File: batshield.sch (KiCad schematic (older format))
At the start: 79 parts, among them J1 mic in, J10 rigth donw pins, J11 service power, J2 Audio-Jack-2, J3 Audio-Jack-2, J4 left uppins, J5 left down pins, J6 Audio-Jack-2, J7 DIN-5_180degree, J8 DIN-5_180degree, J9 rigth up pins, SW1 SW_SPDT, SW10 SW_SPST, SW11 SW_SPST, SW12 SW_Push, SW2 SW_SPDT, SW3 SW_SPDT, SW4 SW_SPST, SW5 SW_Push, SW6 SW_SPST, SW7 SW_Push, SW8 SW_SPST, SW9 SW_Push, U1 LM741, U2 4N35

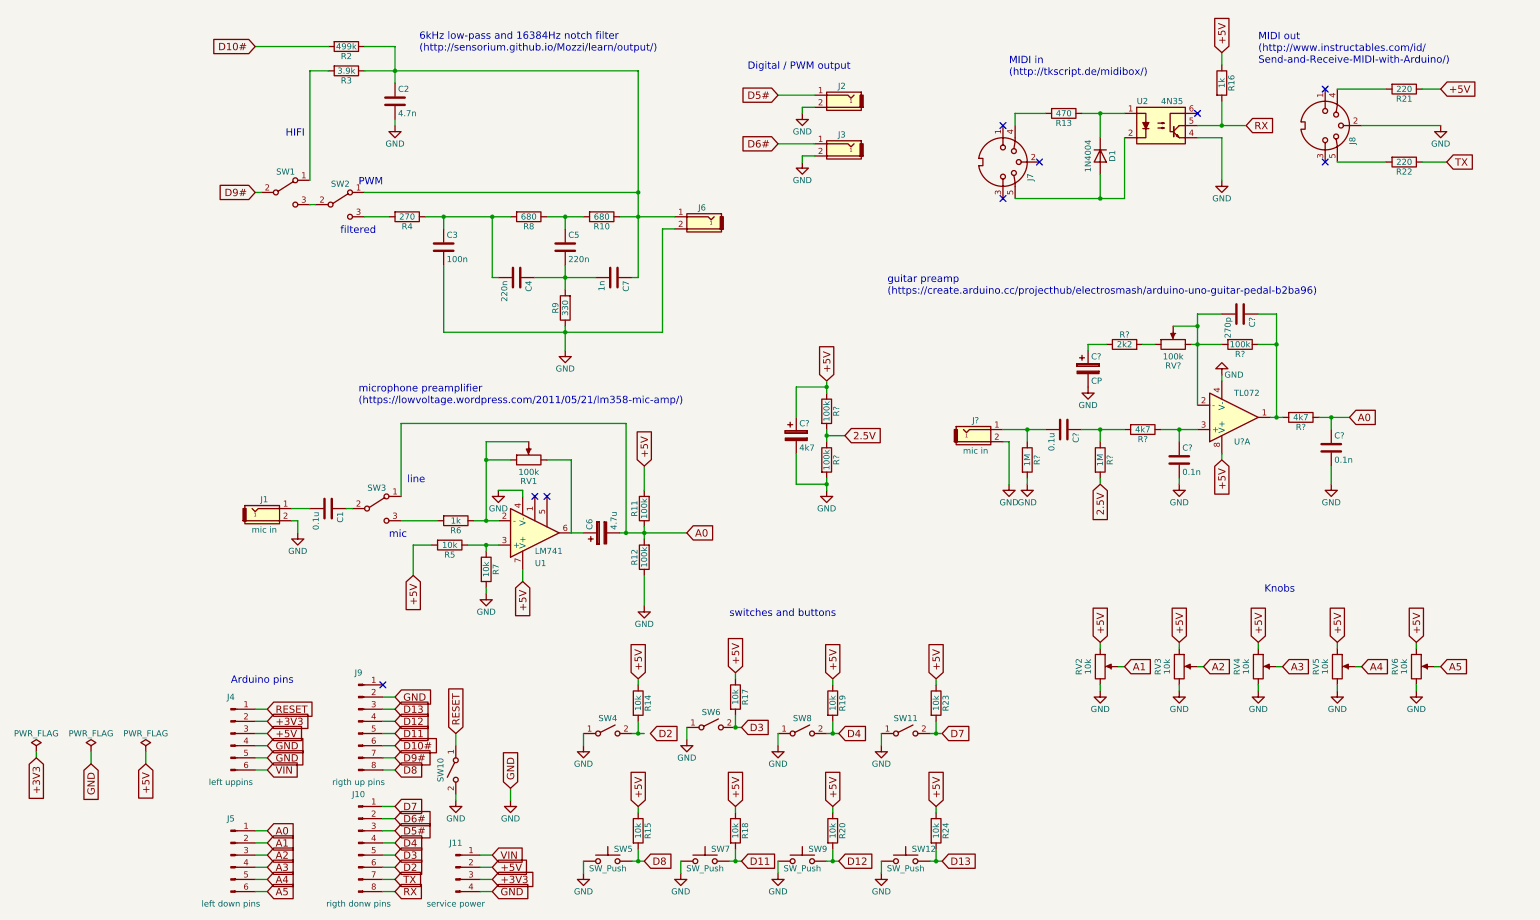
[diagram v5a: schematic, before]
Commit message: simulaciones spice y preamplificador per tutto ii
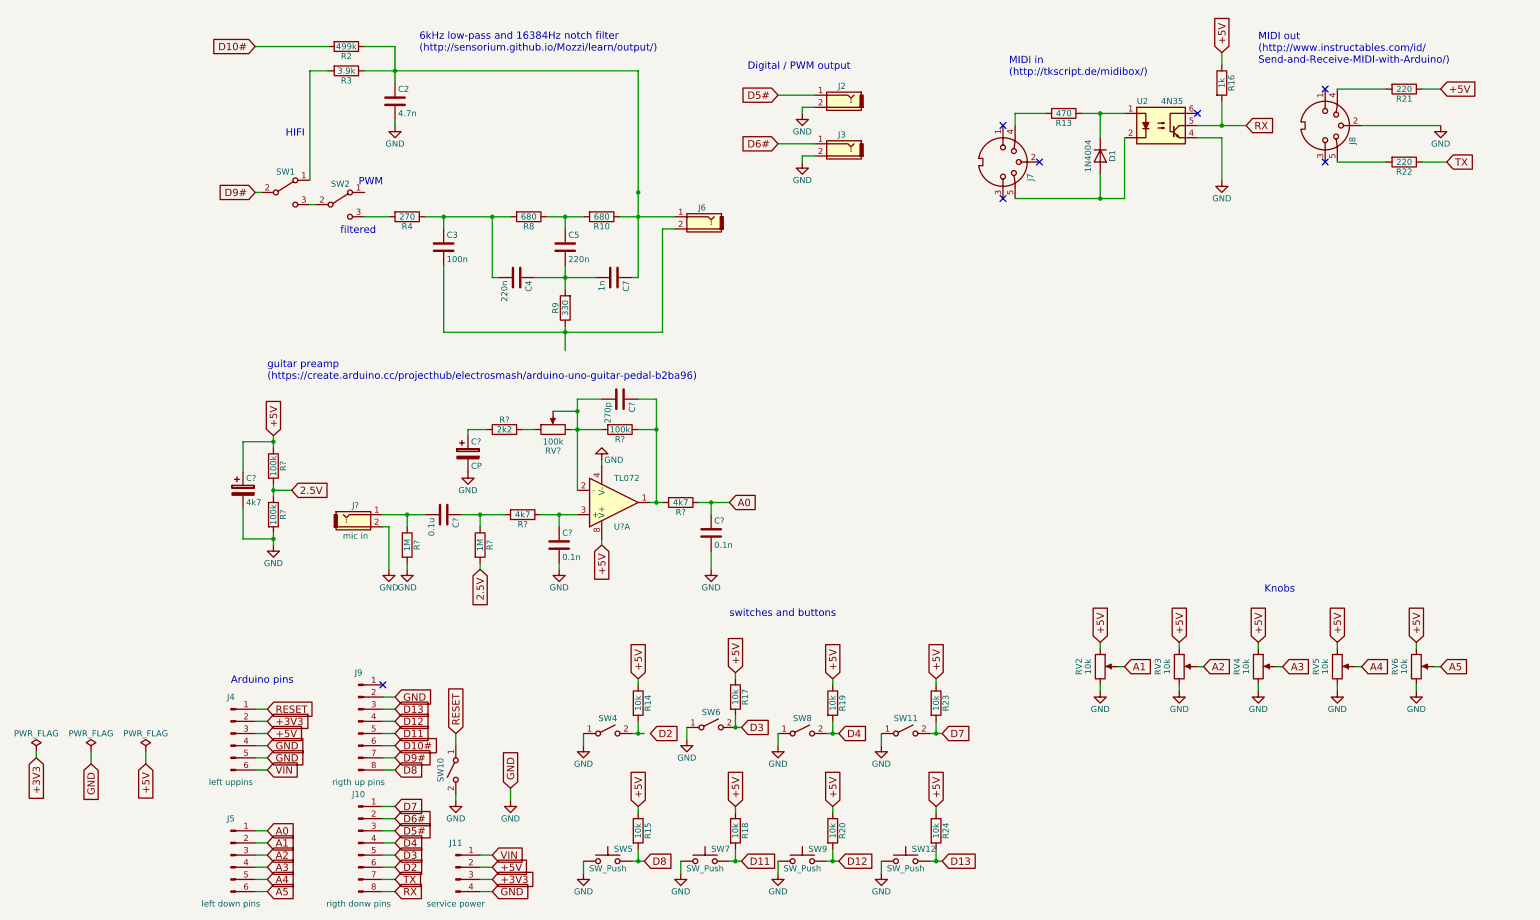
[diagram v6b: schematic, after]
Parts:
- removed C1: 0.1u, symbol C
- removed C6: 4.7u, symbol CP
- removed J1: mic in, symbol Audio-Jack-2
- removed R11, R12: 100k, symbol R
- removed R5, R7: 10k, symbol R
- removed R6: 1k, symbol R
- removed RV1: 100k, symbol POT
- removed SW3: SW_SPDT, symbol SW_SPDT
- removed U1: LM741, symbol LM741
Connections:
- net GND: no longer C3.2, J6.2, R9.1
- net at C2.1, C7.1, J6.1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: no longer SW2.1 (A)
- new net: C3.2, J6.2, R9.1
- no-connect marks 9 -> 7
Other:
- note removed: "line"
- note removed: "mic"
- note removed: "microphone preamplifier\n(https://lowvoltage.wordpress.com/2011/05/21/lm358-mic-amp/)"
- moved on the sheet: C?, J?, R?, RV?, U?A

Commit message: listo para prototipo con breadboard
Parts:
- gave numbers to parts that had none: 17
- renumbered C4 to C10, C7 to C11, C3 to C8, C5 to C9, J2 to J1, J5 to J10, J3 to J2, J6 to J4, J8 to J5, J7 to J6, J9 to J7, J4 to J8, J10 to J9, R2 to R1, R8 to R10, R10 to R11, R9 to R14, R16 to R15, R13 to R16, R21 to R17, R22 to R18, R17 to R19, R3 to R2, R14 to R20, R19 to R21, R23 to R22, R15 to R23, R18 to R24, R20 to R25, R24 to R26, R4 to R9, SW12 to SW10, SW10 to SW11, SW6 to SW3, SW8 to SW5, SW11 to SW6, SW5 to SW7, SW7 to SW8
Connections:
- net D2: now also R20.2, SW4.2 (B)
- net GND: now also C8.2, J4.2, R14.1
- net at C11.1, C2.1, J4.1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: now also SW2.1 (A)
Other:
- moved on the sheet: C1, C10, C11, C2, C3, C4, C5, C6, C7, C8, C9, D1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

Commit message: mejoras, mejoras, mejoras
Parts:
- removed J1, J2: Audio-Jack-2, symbol Audio-Jack-2
- removed J10: left down pins, symbol Conn_01x06_Male
- removed J11: service power, symbol Conn_01x04_Male
- removed J7: rigth up pins, symbol Conn_01x08_Male
- removed J8: left uppins, symbol Conn_01x06_Male
- removed J9: rigth donw pins, symbol Conn_01x08_Male
- removed R15: 1k, symbol R
- removed R22: 10k, symbol R
- removed SW10: SW_Push, symbol SW_Push
- removed SW11, SW6: SW_SPST, symbol SW_SPST
- removed U2: 4N35, Housings_DIP:DIP-6_W7.62mm, symbol 4N25
- added J1, J4: I/O 1, symbol Conn_01x03_Male
- added J2: arduinoUnoPinout, symbol arduinoUnoPinout
- added J5: mic in, symbol Audio-Jack-2
- added J7: Audio-Jack-2, symbol Audio-Jack-2
- added Q1: 2N3904, TO_SOT_Packages_THT:TO-92_Molded_Narrow, symbol 2N3904
- added R21: 220, symbol R
- added R25: 4k7, symbol R
- added SW1: RESET, symbol SW_Push
- added SW2: SOFT/HARD SERIAL READ, symbol SW_SPDT
- added SW3: SOFT/HARD SERIAL WRITE, symbol SW_SPDT
- added SW4: RUN/PROG, symbol SW_SPDT
- added SW7: NORMAL/BRIGHT, symbol SW_SPDT
- added U2: 6N138, Housings_DIP:DIP-8_W7.62mm, symbol 6N138
- C1: footprint (none) -> Capacitors_THT:C_Disc_D5.0mm_W2.5mm_P5.00mm
- C2: renamed from C3; value CP -> 4.7u
- C3: renamed from C4; footprint (none) -> Capacitors_THT:C_Disc_D5.0mm_W2.5mm_P2.50mm
- C4: renamed from C5; value 4k7 -> 4.7u
- C7: renamed from C2; footprint (none) -> Capacitors_THT:C_Disc_D5.0mm_W2.5mm_P5.00mm
- R22: renamed from R16; value 470 -> 220
- R26: value 10k -> 500
- SW5: renamed from SW1; value SW_SPDT -> HIFI/LOFI
- SW6: renamed from SW2; value SW_SPDT -> PWM/FILTERED
- renumbered C11 to C10, C8 to C11, C6 to C5, C7 to C6, C9 to C8, C10 to C9, J4 to J6, J5 to J8, J6 to J9, R3 to R1, R2 to R10, R9 to R11, R10 to R12, R11 to R13, R20 to R14, R19 to R15, R21 to R16, R14 to R17, R23 to R18, R24 to R19, R4 to R2, R25 to R20, R18 to R23, R17 to R24, R5 to R3, R6 to R4, R7 to R5, R8 to R6, R12 to R7, R13 to R8, R1 to R9, SW5 to SW10, SW7 to SW11, SW8 to SW12, SW9 to SW13, SW4 to SW8, SW3 to SW9
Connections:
- net D13 is gone; now on net GND: R26.2
- net TX is gone; now on an unnamed net: R23.1
- net +5V: now also R24.2, J1.2 (Pin_2), J2.4 (5V), J4.2 (Pin_2), Q1.3 (C), R21.1, U2.8; no longer R24.1, R26.1
- net GND: now also J1.1 (Pin_1), J2.28 (GND), J2.5 (GND), J2.6 (GND), J4.1 (Pin_1), J5.2, J7.2, R25.2, SW1.1, U2.5
- net at C11.1, C9.2, R11.1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: now also SW7.3 (C)
- net at R11.2: now also SW7.1 (A); no longer SW6.3 (C)
- net at C10.1, C7.1, J6.1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: now also J7.1
- net at D1.1 (K), R22.1: now also U2.2
- net at D1.2 (A), J9.5: now also U2.3
- net at J8.4: now also R24.1; no longer R24.2
- net at J8.5: no longer R23.2
- net at C3.2, J3.1, R7.1: now also J5.1
- net A0 renamed IN
- net IN: now also J2.8 (A0)
- net A1 renamed KNOB1
- net KNOB1: now also J2.9 (A1)
- net A2 renamed KNOB2
- net KNOB2: now also J2.10 (A2)
- net A3 renamed KNOB3
- net KNOB3: now also J2.11 (A3)
- net A4 renamed KNOB4
- net KNOB4: now also J2.12 (A4)
- net A5 renamed KNOB5
- net KNOB5: now also J2.13 (A5)
- net D10# renamed PWM2
- net PWM2: now also J2.24 (D10)
- net D11 renamed BTN2
- net BTN2: now also J2.19 (D5)
- net D12 renamed BTN3
- net BTN3: now also J2.21 (D7)
- net D2 renamed SWT1
- net SWT1: now also J2.22 (D8)
- net D3 renamed SWT2
- net SWT2: now also J2.26 (D12)
- net D4 renamed SWT3
- net SWT3: now also J2.27 (D13)
- net D8 renamed BTN1
- net BTN1: now also J2.18 (D4)
- net D9# renamed PWM1
- net PWM1: now also J2.23 (D9)
- new net: SW6.3 (C), SW7.2 (B)
- new net: Q1.1 (E), R23.2, R26.1
- new net: R25.1, U2.7
- new net: J2.14 (RX), SW4.2 (B)
- new net: J2.2 (RESET), SW1.2
- new net HARD-RX: SW2.3 (C), SW4.1 (A)
- new net HARD-TX: J2.15 (TX), SW3.3 (C)
- new net IO1: J1.3 (Pin_3), J2.20 (D6)
- new net IO2: J2.25 (D11), J4.3 (Pin_3)
- new net PORT-RX: R21.2, SW2.2 (B), U2.6
- new net PORT-TX: Q1.2 (B), SW3.2 (B)
- new net SOFT-RX: J2.16 (D2), SW2.1 (A)
- new net SOFT-TX: J2.17 (D3), SW3.1 (A)
- no-connect marks 7 -> 10
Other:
- note added: "0.5%"
- note added: "6kHz low-pass and\n16384Hz notch filter"
- note added: "Input"
- note added: "Input / Output"
- note added: "MIDI in"
- note added: "MIDI out"
- note added: "Output"
- note added: "SW2 y SW3 select betwwen hardware\nserial port (pins 0 and 1) and software\nserial port (pins 2 and 3)"
- note added: "Shield connections and control"
- note added: "buttons"
- note added: "if using hardware serial, set SW4 OFF \nwhen uploading program to Arduino"
- note added: "jack 1/4''"
- note added: "jack 1/8''"
- note added: "knobs"
- note added: "switches"
- note removed: "6kHz low-pass and 16384Hz notch filter\n(http://sensorium.github.io/Mozzi/learn/output/)"
- note removed: "Arduino pins"
- note removed: "Digital / PWM output"
- note removed: "MIDI in\n(http://tkscript.de/midibox/)"
- note removed: "MIDI out\n(http://www.instructables.com/id/\nSend-and-Receive-MIDI-with-Arduino/)"
- note removed: "PWM\n"
- note removed: "filtered"
- note removed: "guitar preamp\n(https://create.arduino.cc/projecthub/electrosmash/arduino-uno-guitar-pedal-b2ba96)"
- note removed: "switches and buttons"
- moved on the sheet: C1, C10, C11, C2, C3, C4, C5, C6, C7, C8, C9, D1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
